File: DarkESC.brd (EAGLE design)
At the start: 83.3 x 79.7 mm, 98 parts, among them IC1 7805DT, IC2 ACS712ELCTR-20A-T, Q1 BC817-40W, Q2 BC817-40W, Q3 BC817-40W, Q4 IRF520, Q5 IRF520, Q6 IRF520, Q7 IRF520, Q8 IRF520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

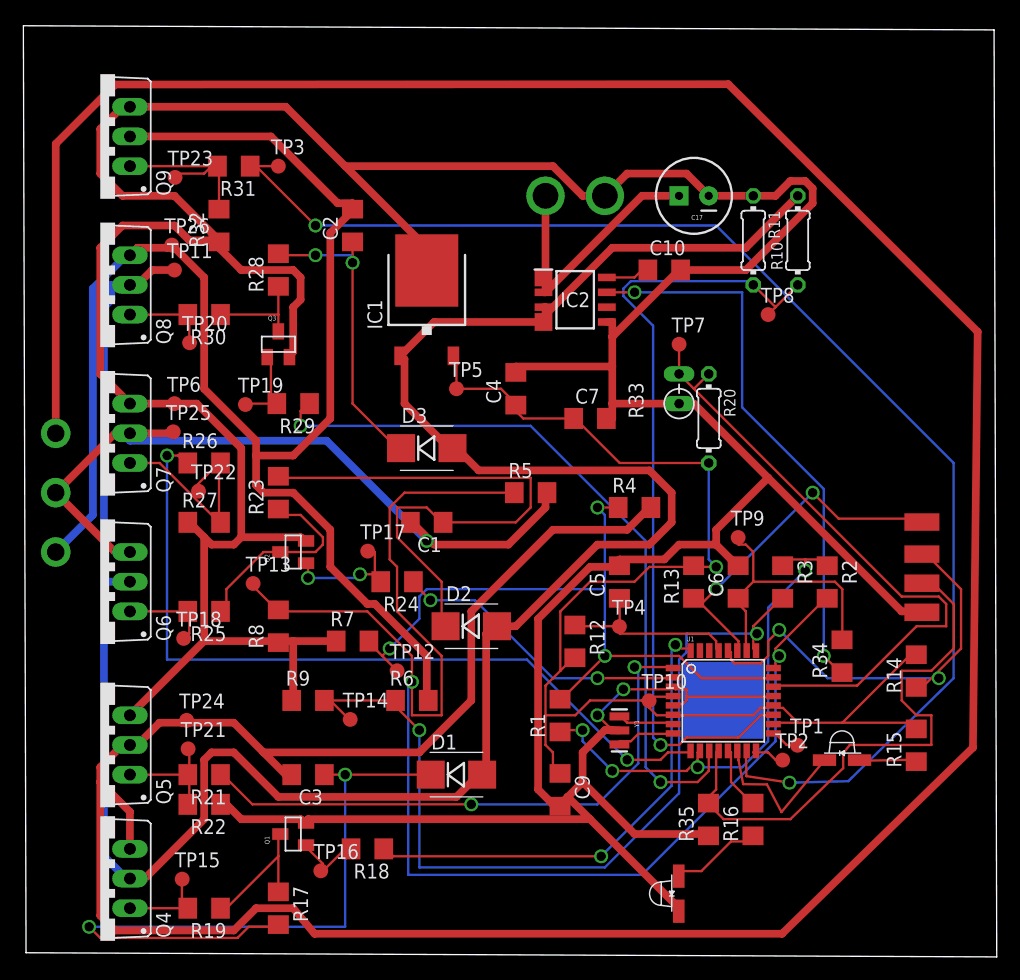
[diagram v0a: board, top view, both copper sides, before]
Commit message: Updated Power Lines
Updated Power Lines with Thicker Rails
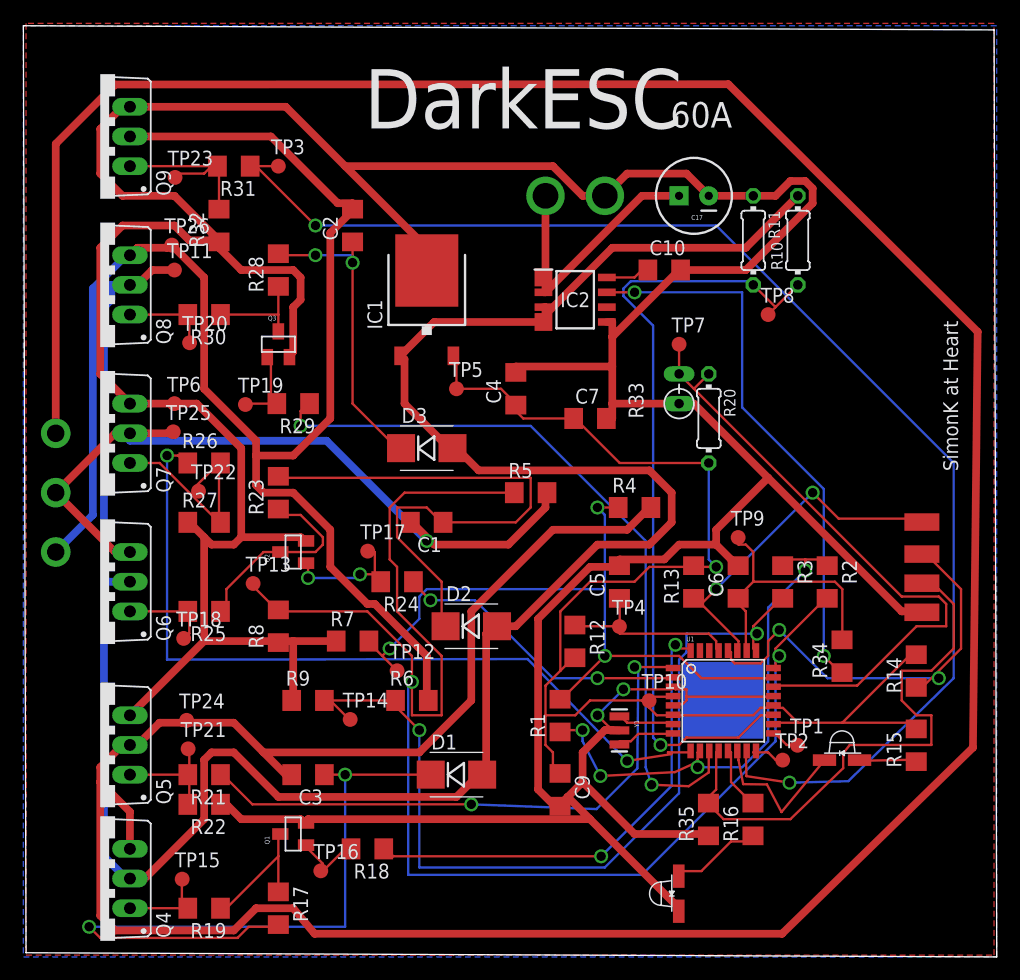
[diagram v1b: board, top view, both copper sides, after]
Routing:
- net CENTER: track 44.0 -> 44.6 mm
- net PWM_CH: track 63.3 -> 64.0 mm
- net PWM_BL: track 68.2 -> 68.7 mm
- added copper zone on layer 1, net N$1
- added copper zone on layer 16, net N$8
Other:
- board text added: "60A"
- board text added: "DarkESC"
- board text added: "SimonK at Heart"
